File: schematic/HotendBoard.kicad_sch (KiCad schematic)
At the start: 0 parts

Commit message: Progress on KiCAD schematics
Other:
- title: (none) -> Da Vinci Jr. 1.0 Hotend Board schematic
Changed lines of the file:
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@@
 	(generator_version "10.0")
 	(paper "A4")
+	(title_block
+		(title "Da Vinci Jr. 1.0 Hotend Board schematic")
+		(date "2026-08-26")
+		(rev "1")
+	)
 )

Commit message: Add hotend board schematic
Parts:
- added J1: NOZZ/FAN/NTC/SW, symbol Connector:Conn_01x51_Pin
- added J2: Fan, symbol Connector:Conn_01x02_Pin
- added J3: NTC, symbol Connector:Conn_01x02_Pin
- added J4: Conn_01x02_Pin, symbol Connector:Conn_01x02_Pin
- added J4: Heater, symbol Connector:Conn_01x02_Pin
- added J5: Unknown, symbol Connector:Conn_01x02_Pin
- added R1: 560ohm, Resistor_THT:R_Axial_DIN0207_L6.3mm_D2.5mm_P10.16mm_Horizontal, symbol PCM_SL_Resistors:560ohm
- added U1-1: (no value), symbol Device:LED
- added U1-2: (no value), OptoDevice:Kingbright_KPS-3227, symbol Sensor_Optical:KPS-3227
- added U3: AT24CS01-SSHM, Package_SO:SOIC-8_3.9x4.9mm_P1.27mm, symbol Memory_EEPROM:AT24CS01-SSHM
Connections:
- new net: J1.23 (Pin_23), J1.24 (Pin_24), U3.5 (SDA)
- new net: J1.27 (Pin_27), J1.28 (Pin_28), U3.6 (SCL)
- new net: J1.25 (Pin_25), J1.26 (Pin_26), U3.8 (VCC)
- new net: R1.1, U1-2.1, U1-2.3
- new net: J1.33 (Pin_33), J1.34 (Pin_34), J5.1 (Pin_1)
- new net: J1.16 (Pin_16), J1.17 (Pin_17), J2.1 (Pin_1)
- new net: J1.30 (Pin_30), J1.31 (Pin_31), J3.1 (Pin_1)
- new net: J1.20 (Pin_20), J1.21 (Pin_21), U1-1.2 (A)
- new net: J1.38 (Pin_38), J1.39 (Pin_39), J1.40 (Pin_40), J1.41 (Pin_41), J1.42 (Pin_42), J1.43 (Pin_43), J4.1 (Pin_1)
- new net GNDREF: J1.19 (Pin_19), J1.22 (Pin_22), J1.29 (Pin_29), J1.32 (Pin_32), J1.46 (Pin_46), J1.47 (Pin_47), J1.48 (Pin_48), J1.49 (Pin_49), J1.50 (Pin_50), J1.51 (Pin_51), J2.2 (Pin_2), J3.2 (Pin_2), J4.2 (Pin_2), J5.2 (Pin_2), U1-1.1 (K), U1-2.2, U1-2.4, U3.1 (A0), U3.2 (A1), U3.3 (A2), U3.4 (GND), U3.7 (WP)
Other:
- note added: "U1"

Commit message: Update board schematics
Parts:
- U3: value AT24CS01-SSHM -> AT24C02D
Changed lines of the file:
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@@
 			)
 		)
-		(property "Value" "AT24CS01-SSHM"
+		(property "Value" "AT24C02D"
 			(at 135.1981 60.96 0)
 			(show_name no)

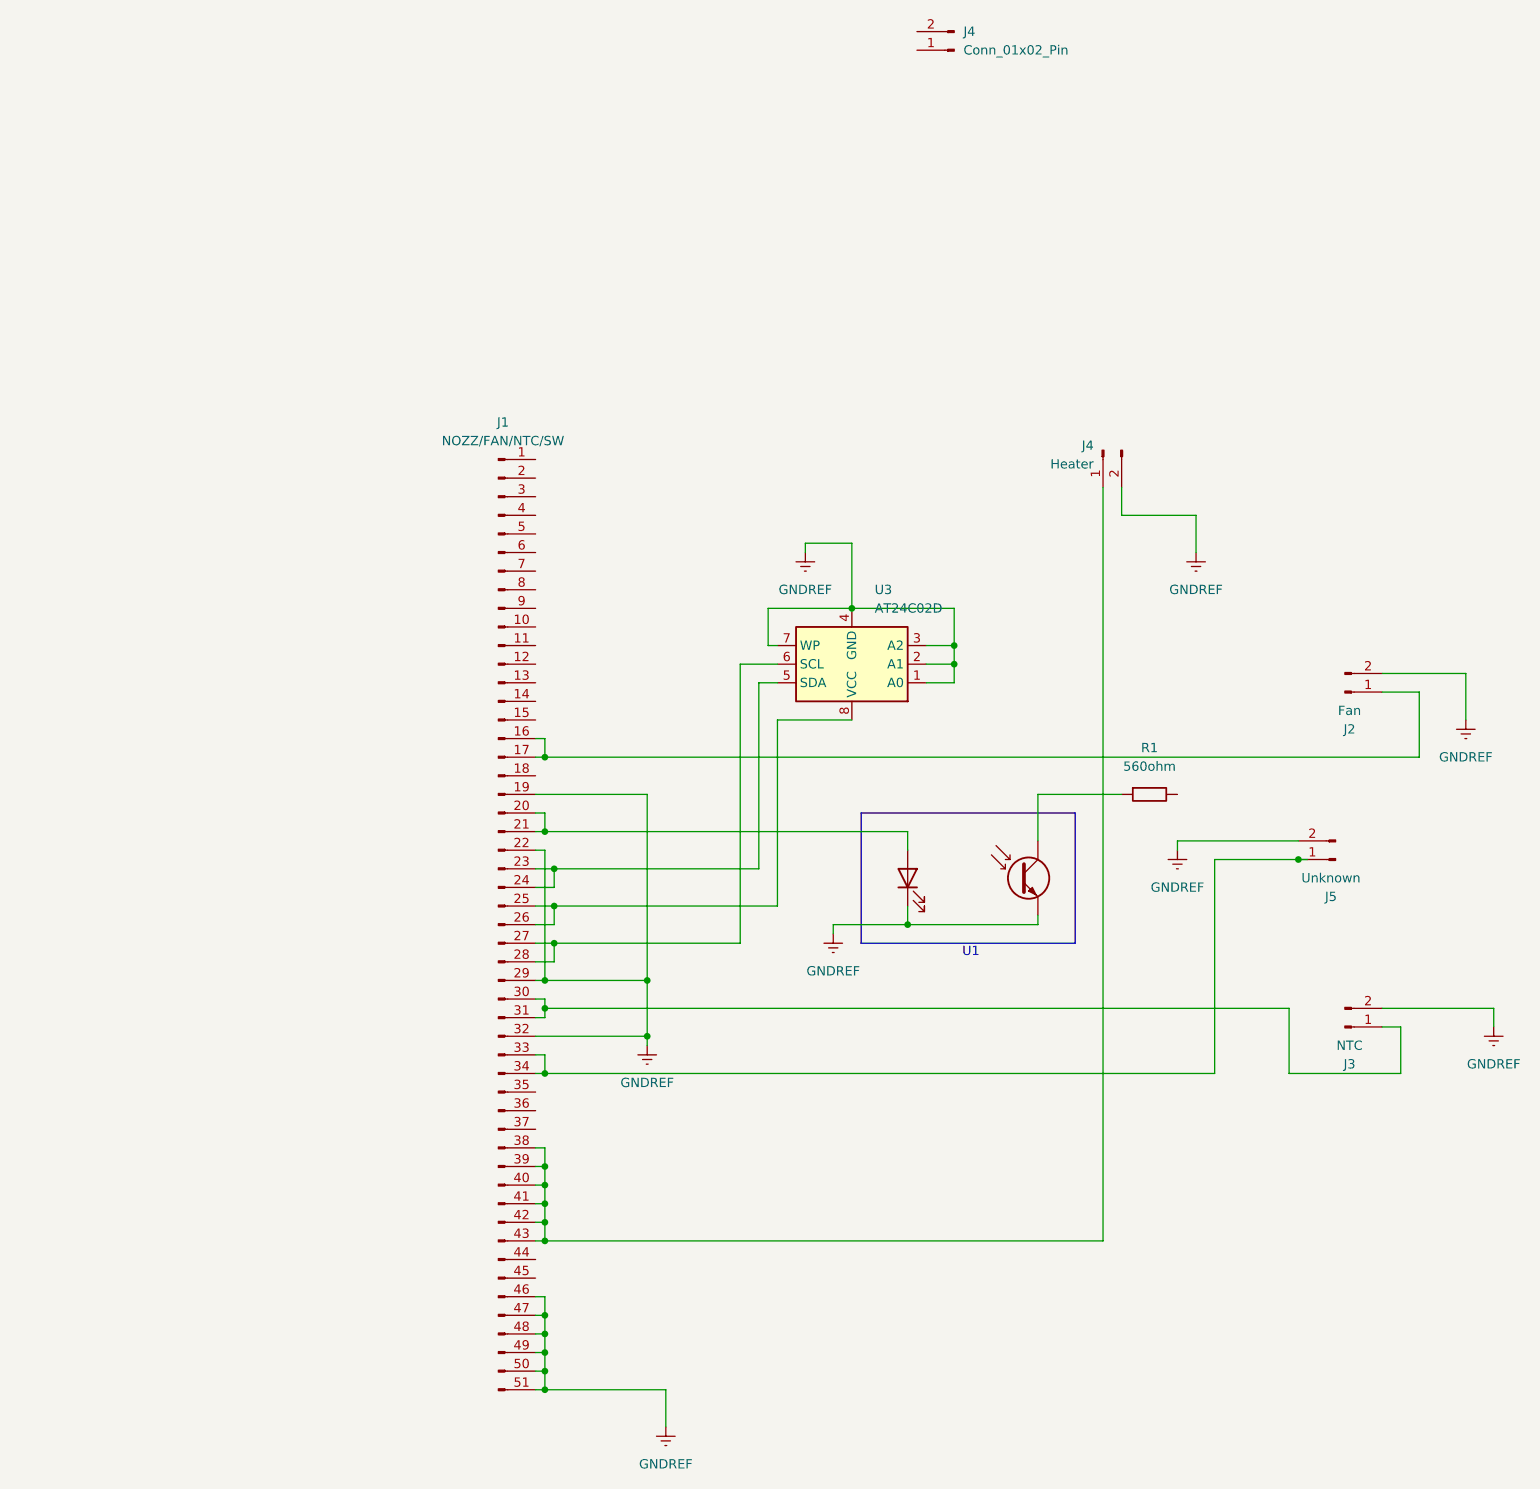
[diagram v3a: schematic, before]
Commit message: Start main board schematic and update hotend schematic size
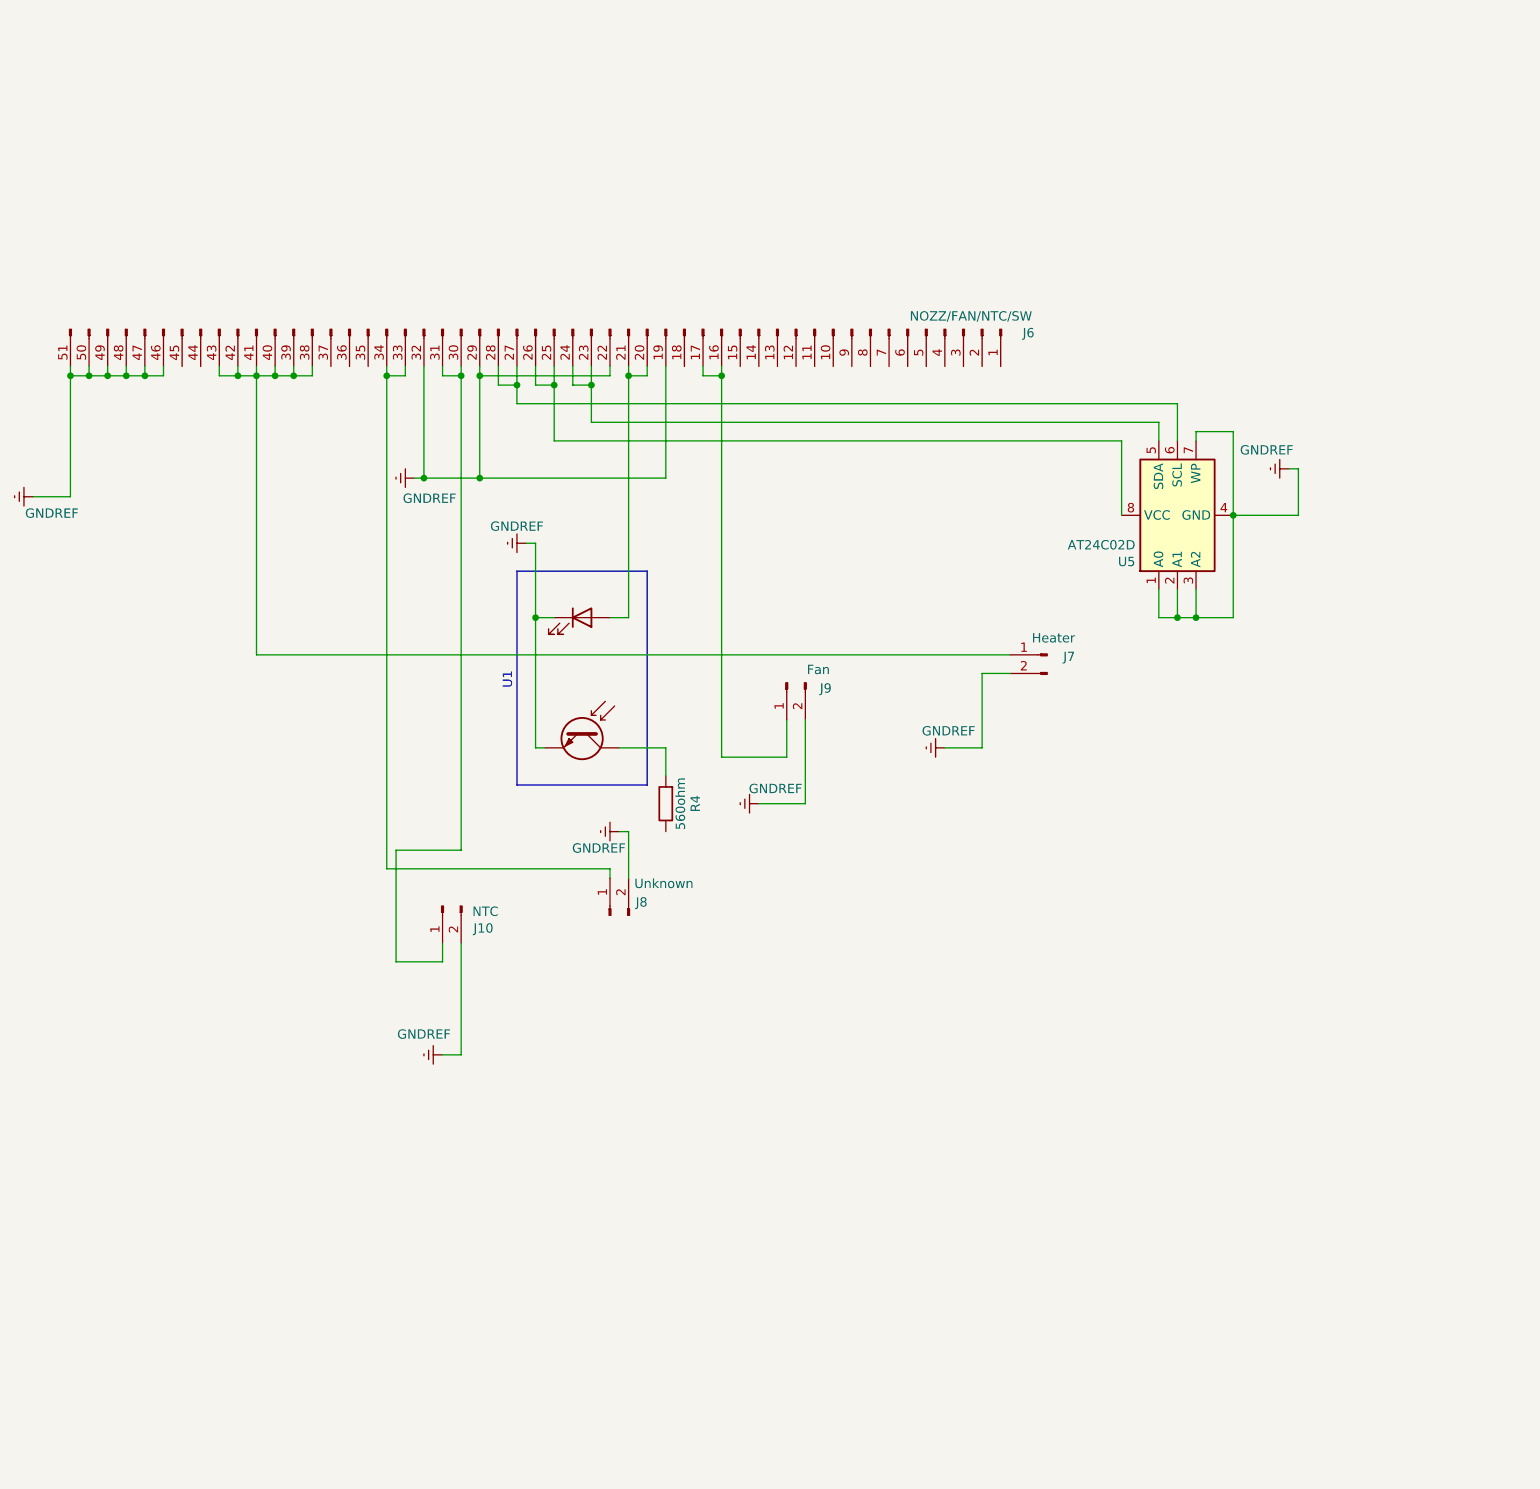
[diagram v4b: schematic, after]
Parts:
- removed J1: NOZZ/FAN/NTC/SW, symbol Connector:Conn_01x51_Pin
- removed J2: Fan, symbol Connector:Conn_01x02_Pin
- removed J3: NTC, symbol Connector:Conn_01x02_Pin
- removed J4: Conn_01x02_Pin, symbol Connector:Conn_01x02_Pin
- removed J4: Heater, symbol Connector:Conn_01x02_Pin
- removed J5: Unknown, symbol Connector:Conn_01x02_Pin
- removed R1: 560ohm, Resistor_THT:R_Axial_DIN0207_L6.3mm_D2.5mm_P10.16mm_Horizontal, symbol PCM_SL_Resistors:560ohm
- removed U1-1: (no value), symbol Device:LED
- removed U1-2: (no value), OptoDevice:Kingbright_KPS-3227, symbol Sensor_Optical:KPS-3227
- removed U3: AT24C02D, Package_SO:SOIC-8_3.9x4.9mm_P1.27mm, symbol Memory_EEPROM:AT24CS01-SSHM
- added J10: NTC, symbol Connector:Conn_01x02_Pin
- added J6: NOZZ/FAN/NTC/SW, symbol Connector:Conn_01x51_Pin
- added J7: Heater, symbol Connector:Conn_01x02_Pin
- added J8: Unknown, symbol Connector:Conn_01x02_Pin
- added J9: Fan, symbol Connector:Conn_01x02_Pin
- added R4: 560ohm, Resistor_THT:R_Axial_DIN0207_L6.3mm_D2.5mm_P10.16mm_Horizontal, symbol PCM_SL_Resistors:560ohm
- added U1-3: (no value), symbol Device:LED
- added U1-4: (no value), OptoDevice:Kingbright_KPS-3227, symbol Sensor_Optical:KPS-3227
- added U5: AT24C02D, Package_SO:SOIC-8_3.9x4.9mm_P1.27mm, symbol Memory_EEPROM:AT24CS01-SSHM
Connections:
- net GNDREF: now also J10.2 (Pin_2), J6.19 (Pin_19), J6.22 (Pin_22), J6.29 (Pin_29), J6.32 (Pin_32), J6.46 (Pin_46), J6.47 (Pin_47), J6.48 (Pin_48), J6.49 (Pin_49), J6.50 (Pin_50), J6.51 (Pin_51), J7.2 (Pin_2), J8.2 (Pin_2), J9.2 (Pin_2), U1-3.1 (K), U1-4.2, U1-4.4, U5.1 (A0), U5.2 (A1), U5.3 (A2), U5.4 (GND), U5.7 (WP)
- new net: J6.16 (Pin_16), J6.17 (Pin_17), J9.1 (Pin_1)
- new net: J10.1 (Pin_1), J6.30 (Pin_30), J6.31 (Pin_31)
- new net: J6.23 (Pin_23), J6.24 (Pin_24), U5.5 (SDA)
- new net: J6.27 (Pin_27), J6.28 (Pin_28), U5.6 (SCL)
- new net: J6.25 (Pin_25), J6.26 (Pin_26), U5.8 (VCC)
- new net: J6.20 (Pin_20), J6.21 (Pin_21), U1-3.2 (A)
- new net: J6.38 (Pin_38), J6.39 (Pin_39), J6.40 (Pin_40), J6.41 (Pin_41), J6.42 (Pin_42), J6.43 (Pin_43), J7.1 (Pin_1)
- new net: R4.1, U1-4.1, U1-4.3
- new net: J6.33 (Pin_33), J6.34 (Pin_34), J8.1 (Pin_1)

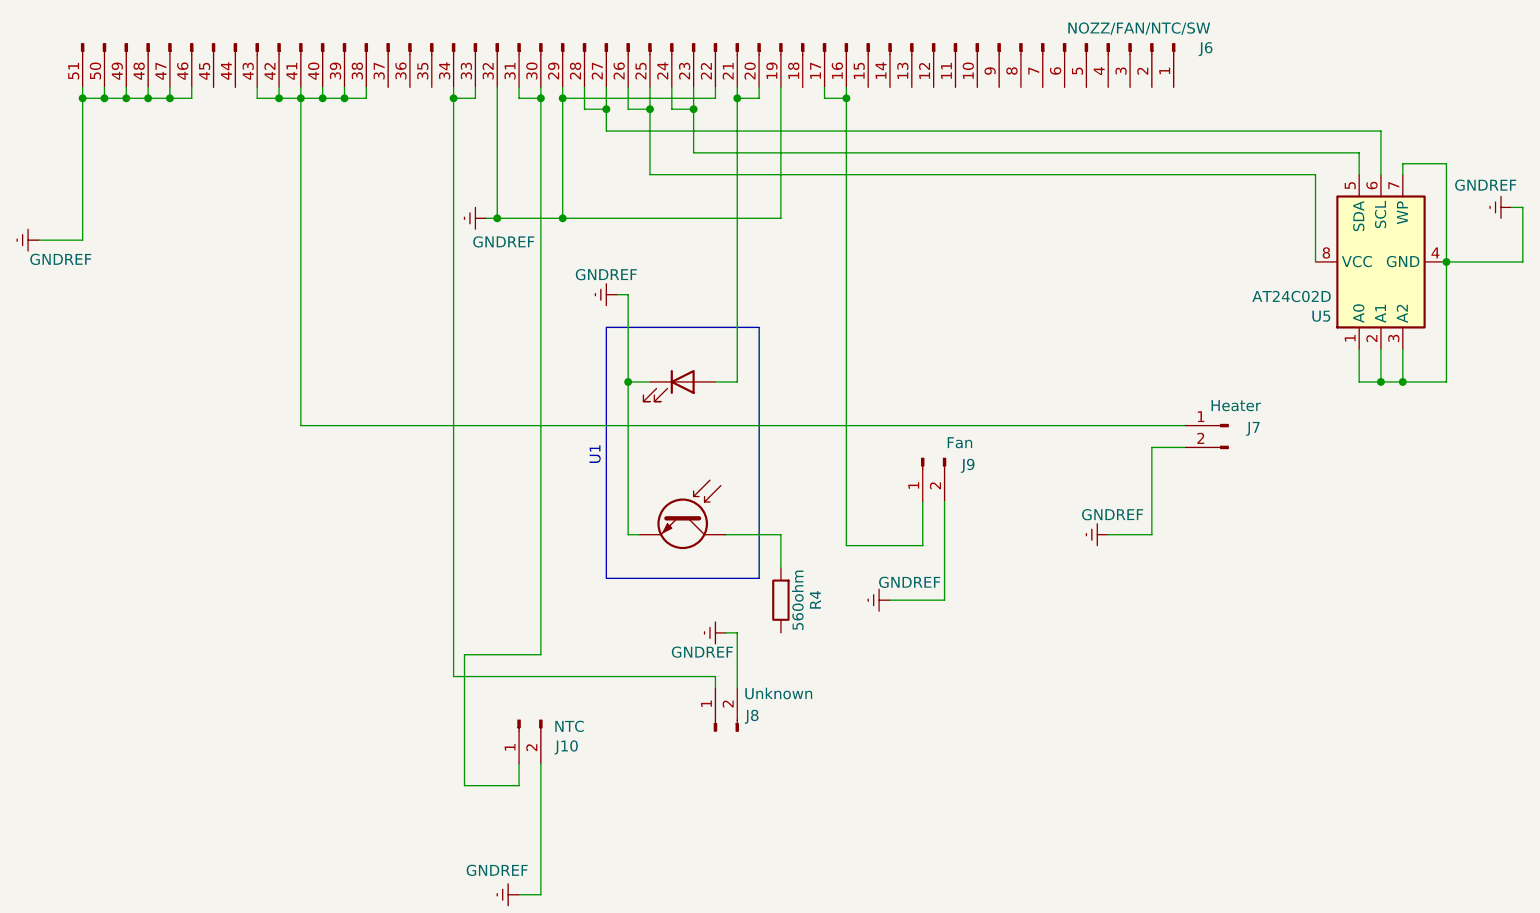
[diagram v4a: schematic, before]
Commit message: Complete hotend documentation and schematics
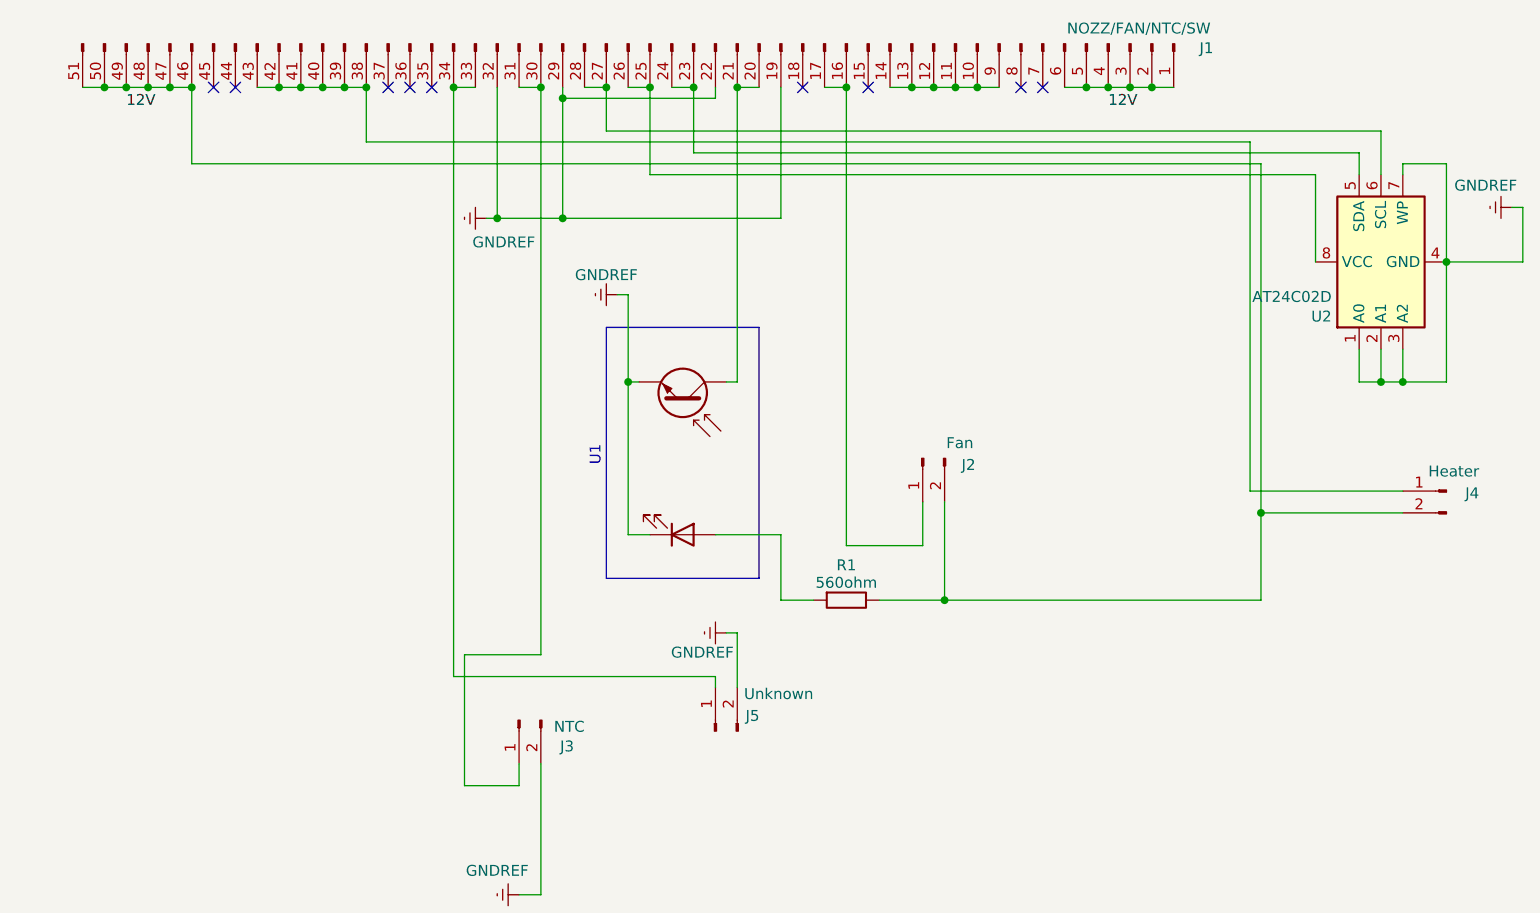
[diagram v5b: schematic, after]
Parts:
- renumbered J6 to J1, J9 to J2, J10 to J3, J7 to J4, J8 to J5, R4 to R1, U5 to U2
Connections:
- net GNDREF: no longer J1.46 (Pin_46), J1.47 (Pin_47), J1.48 (Pin_48), J1.49 (Pin_49), J1.50 (Pin_50), J1.51 (Pin_51), J2.2 (Pin_2), J4.2 (Pin_2)
- net at J1.20 (Pin_20), J1.21 (Pin_21): now also U1-4.1, U1-4.3; no longer U1-3.2 (A)
- net at R1.2: now also J1.46 (Pin_46), J1.47 (Pin_47), J1.48 (Pin_48), J1.49 (Pin_49), J1.50 (Pin_50), J1.51 (Pin_51), J2.2 (Pin_2), J4.2 (Pin_2)
- net at J1.1 (Pin_1): now also J1.2 (Pin_2), J1.3 (Pin_3), J1.4 (Pin_4), J1.5 (Pin_5), J1.6 (Pin_6)
- net at J1.10 (Pin_10): now also J1.11 (Pin_11), J1.12 (Pin_12), J1.13 (Pin_13), J1.14 (Pin_14), J1.9 (Pin_9)
- new net: R1.1, U1-3.2 (A)
- no-connect marks 0 -> 9
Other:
- moved on the sheet: J4, R1
